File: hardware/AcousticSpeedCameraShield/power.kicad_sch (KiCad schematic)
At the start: 22 parts, among them U1 BMS_3S, U2 Charger_3S_USB, U3 StepDown_3.3V_1A, U4 StepDown_5V_1A

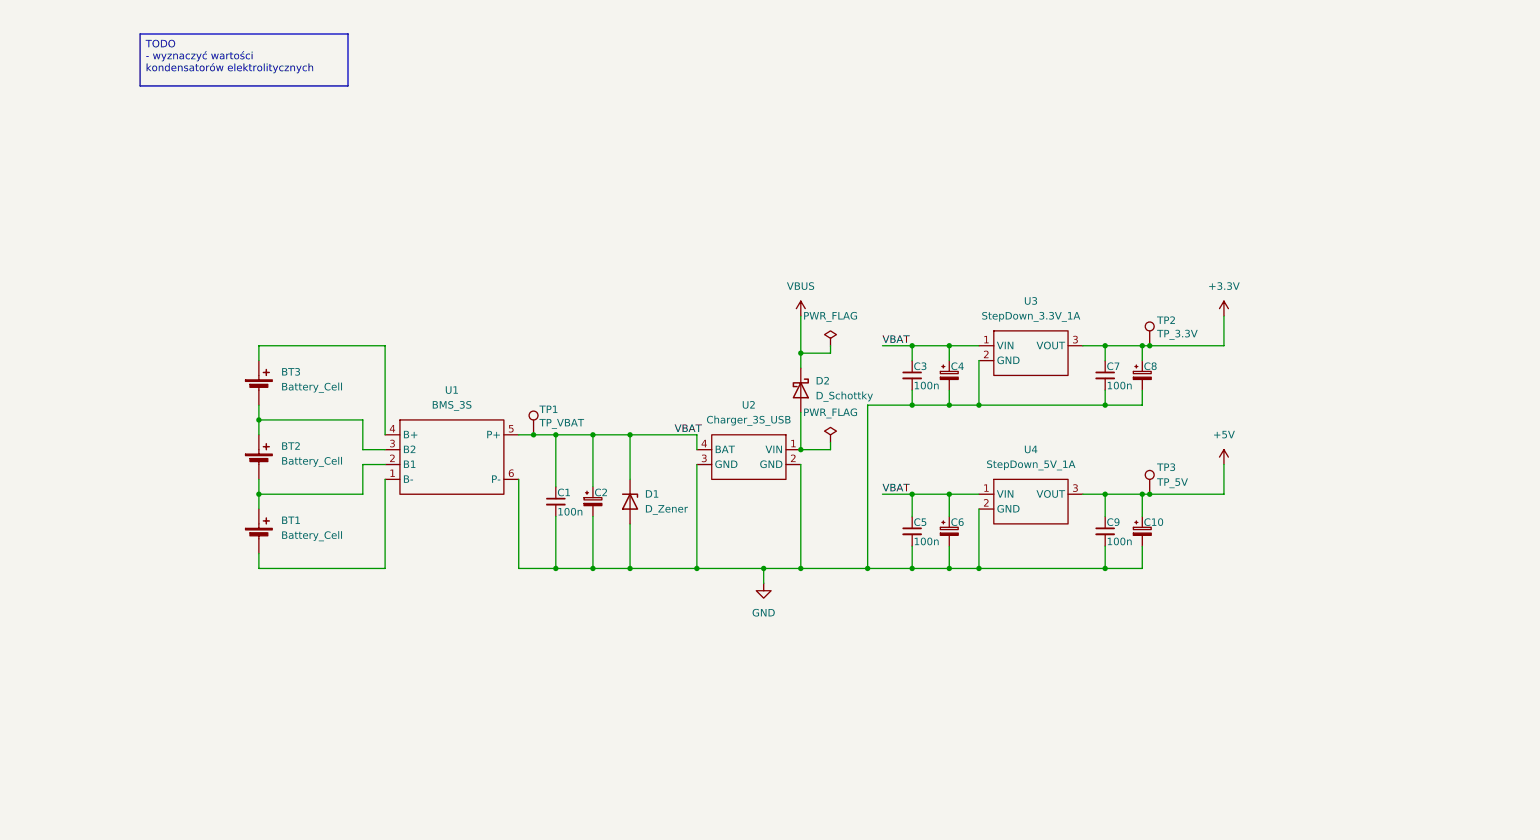
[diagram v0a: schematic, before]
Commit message: update MCU pin assignments
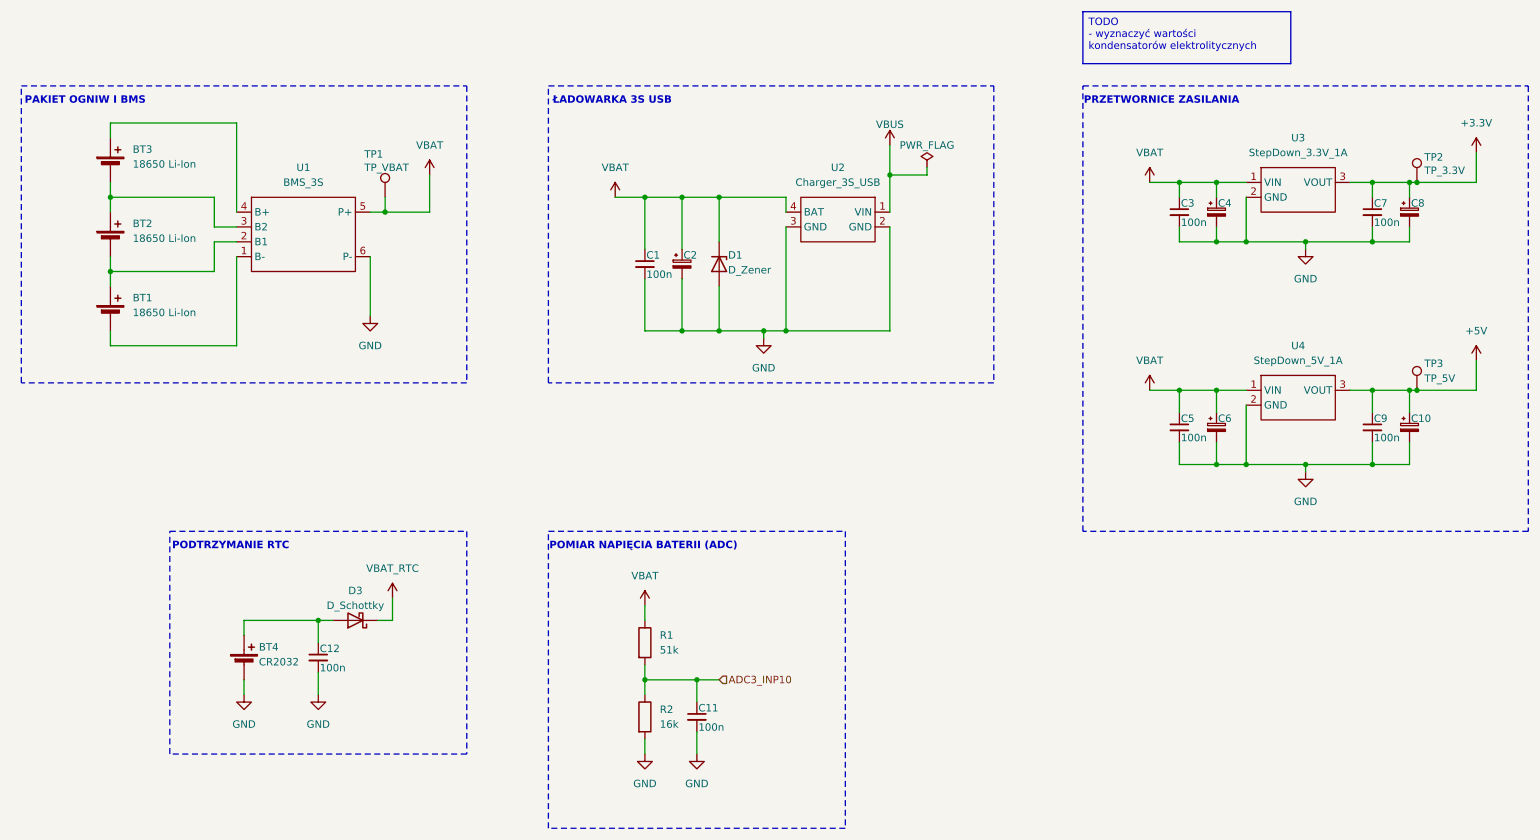
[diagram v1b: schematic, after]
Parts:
- removed D2: D_Schottky, symbol Device:D_Schottky
- added BT4: CR2032, symbol Device:Battery_Cell
- added C11, C12: 100n, symbol Device:C_Small
- added D3: D_Schottky, symbol Device:D_Schottky
- added R1: 51k, symbol Device:R
- added R2: 16k, symbol Device:R
- BT1, BT2, BT3: value Battery_Cell -> 18650 Li-Ion
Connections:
- net GND: now also BT4.2 (-), C11.2, C12.2, R2.2
- net VBAT: now also R1.1
- net VBUS: now also U2.1 (VIN)
- new net: BT4.1 (+), C12.1, D3.2 (A)
- new net ADC3_INP10: C11.1, R1.2, R2.1
- new net VBAT_RTC: D3.1 (K)
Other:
- note added: "PAKIET OGNIW I BMS"
- note added: "PODTRZYMANIE RTC"
- note added: "POMIAR NAPIĘCIA BATERII (ADC)"
- note added: "PRZETWORNICE ZASILANIA"
- note added: "ŁADOWARKA 3S USB"
- title: (none) -> Sekcja Zasilania
- moved on the sheet: BT1, BT2, BT3, C1, C10, C2, C3, C4, C5, C6, C7, C8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
